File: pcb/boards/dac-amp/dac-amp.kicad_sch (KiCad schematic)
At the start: 10 parts, among them J1 I2S_Input, J2 12V_Input, J3 Front_Left, J4 Front_Right, J5 Rear_Left, J6 Rear_Right, U1 PCM5142, U2 TPA3116D2, U3 TPA3116D2, U4 AMS1117-3.3

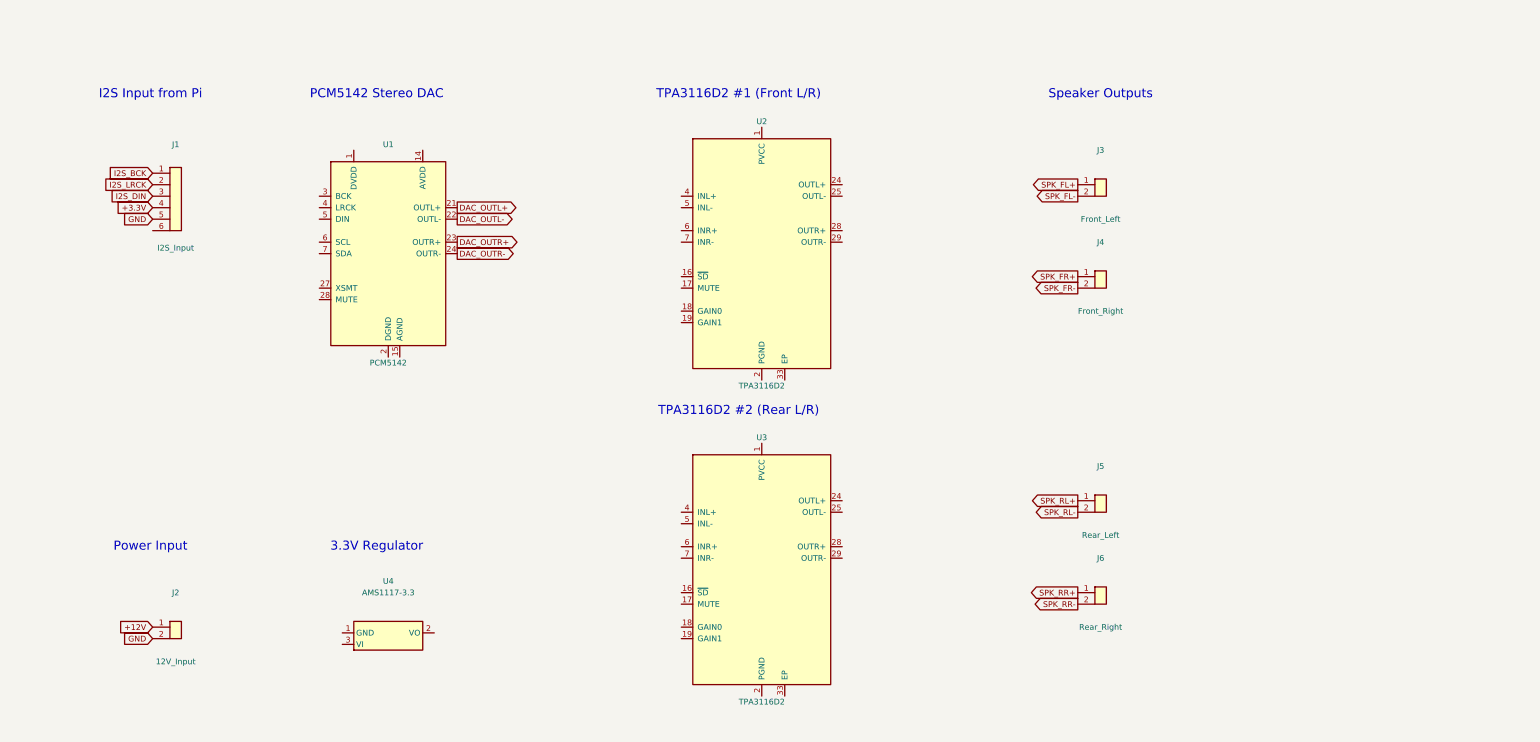
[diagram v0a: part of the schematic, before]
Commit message: Power HAT: Initial PCB layout with component placement
PCB Layout:
- 65mm × 56mm board outline (standard Pi HAT)
- 4× M2.5 mounting holes at corners
- 40-pin GPIO header (J2) positioned for Pi stacking
- Power section (U1 TPS54560, L1, capacitors) on left side
- MCU section (U3 ATtiny85, Y1 crystal) in center
- MOSFET power switching (Q1, Q2, Q3) at bottom
- Optocoupler (U2) for ignition detection

Also includes:
- DAC/Amp HAT schematic complete with I2S, I2C, power wiring
- CAN HAT schematic updates
- Layout scripts for automated component placement
- Updated documentation

Co-Authored-By: Claude Opus 4.5 <noreply@anthropic.com>
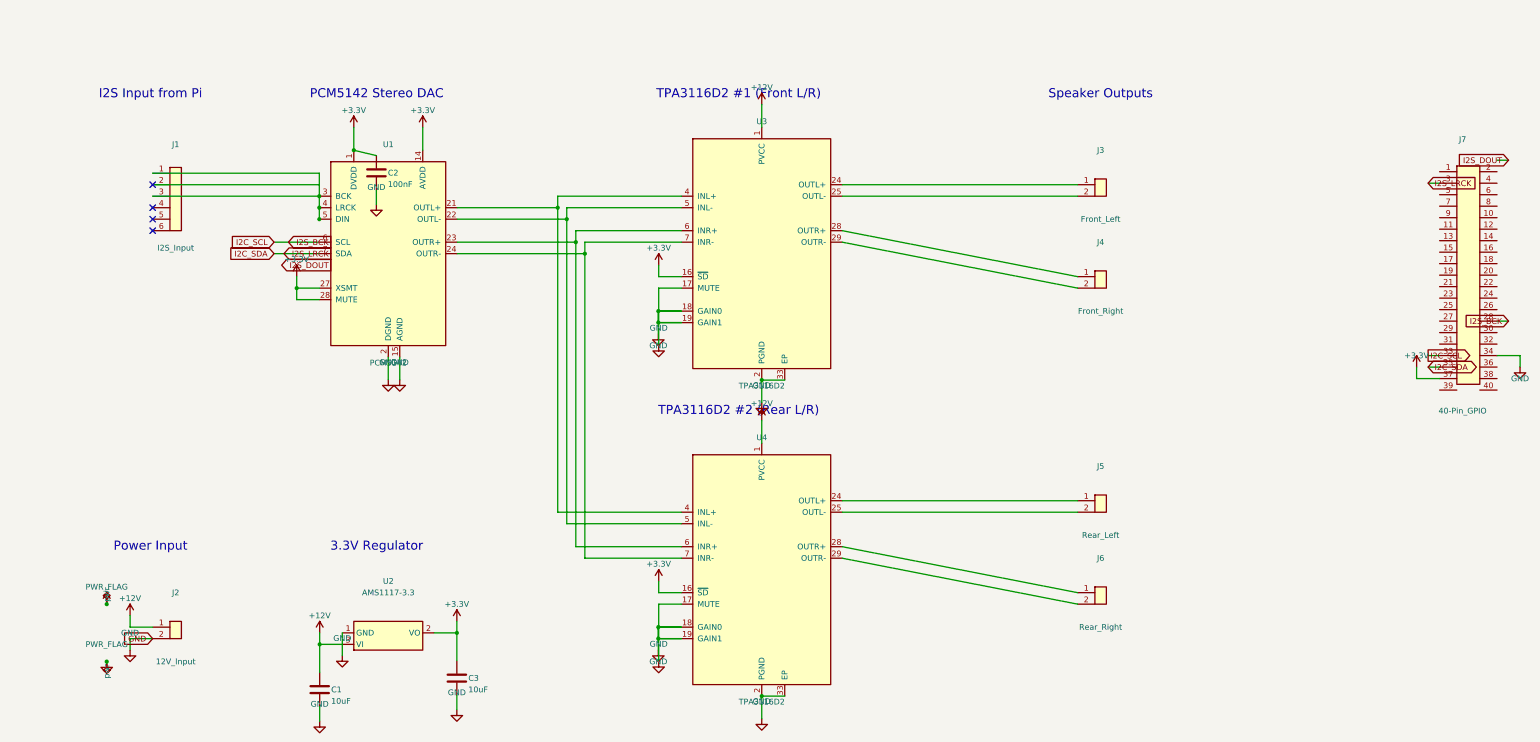
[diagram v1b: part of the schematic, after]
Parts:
- added C1, C3: 10uF, Capacitor_SMD:C_0805_2012Metric, symbol Device:C
- added C2: 100nF, Capacitor_SMD:C_0805_2012Metric, symbol Device:C
- added J7: 40-Pin_GPIO, Connector_PinSocket_2.54mm:PinSocket_2x20_P2.54mm_Vertical, symbol Connector_Generic:Conn_02x20_Odd_Even
- renumbered U4 to U2, U2 to U3, U3 to U4
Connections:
- net DAC_OUTL+ is gone; now on an unnamed net: U1.21 (OUTL+)
- net DAC_OUTL- is gone; now on an unnamed net: U1.22 (OUTL-)
- net DAC_OUTR+ is gone; now on an unnamed net: U1.23 (OUTR+)
- net DAC_OUTR- is gone; now on an unnamed net: U1.24 (OUTR-)
- net I2S_DIN is gone; now on an unnamed net: J1.3 (Pin_3)
- net +12V: now also U2.3 (VI), U3.1 (PVCC), U4.1 (PVCC), C1.1
- net +3.3V: now also U1.1 (DVDD), U1.14 (AVDD), U1.27 (XSMT), U1.28 (MUTE), U2.2 (VO), U3.16 (~{SD}), U4.16 (~{SD}), C2.1, C3.1, J7.37 (Pin_37); no longer J1.4 (Pin_4)
- net GND: now also U1.15 (AGND), U1.2 (DGND), U2.1 (GND), U3.17 (MUTE), U3.18 (GAIN0), U3.19 (GAIN1), U3.2 (PGND), U3.33 (EP), U4.17 (MUTE), U4.18 (GAIN0), U4.19 (GAIN1), U4.2 (PGND), U4.33 (EP), C1.2, C2.2, C3.2, J7.34 (Pin_34); no longer J1.5 (Pin_5)
- net I2S_BCK: now also J7.28 (Pin_28); no longer J1.1 (Pin_1)
- net I2S_LRCK: now also J7.3 (Pin_3); no longer J1.2 (Pin_2)
- net at J5.1 (Pin_1): now also U4.24 (OUTL+)
- net at J5.2 (Pin_2): now also U4.25 (OUTL-)
- net at J4.1 (Pin_1): now also U3.28 (OUTR+)
- net at J4.2 (Pin_2): now also U3.29 (OUTR-)
- net at J6.1 (Pin_1): now also U4.28 (OUTR+)
- net at J6.2 (Pin_2): now also U4.29 (OUTR-)
- net at J3.1 (Pin_1): now also U3.24 (OUTL+)
- net at J3.2 (Pin_2): now also U3.25 (OUTL-)
- net at U3.4 (INL+): now also U4.4 (INL+)
- net at U3.5 (INL-): now also U4.5 (INL-)
- net at U3.6 (INR+): now also U4.6 (INR+)
- net at U3.7 (INR-): now also U4.7 (INR-)
- net at U1.3 (BCK): now also J1.1 (Pin_1), U1.4 (LRCK), U1.5 (DIN)
- net I2C_SCL: now reaches U1.6 (SCL)
- net I2C_SCL: now also J7.33 (Pin_33)
- net I2C_SDA: now reaches U1.7 (SDA)
- net I2C_SDA: now also J7.35 (Pin_35)
- no-connect marks 0 -> 4

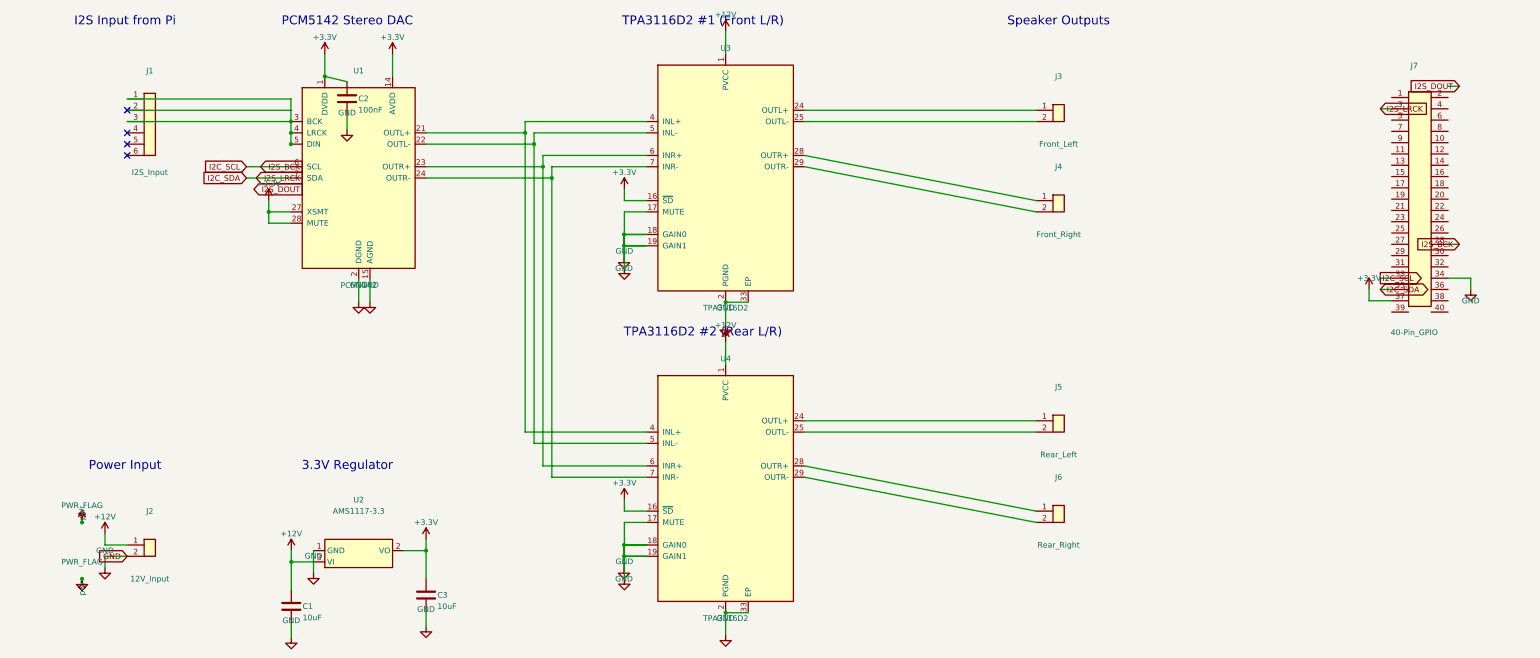
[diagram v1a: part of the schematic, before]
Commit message: CAN HAT + DAC/Amp: PCB layouts started with HAT board outlines
- CAN HAT: PCB created with 65x56mm board outline and M2.5 mounting holes
- DAC/Amp: Fixed remaining ERC errors (XSMT/MUTE tied to 3.3V, J1 no_connect)
- DAC/Amp: Updated TPA3116D2 footprint to ThermalVias variant
- DAC/Amp: PCB created with HAT board outline and mounting holes
- Both boards ready for component placement and routing

Co-Authored-By: Claude Opus 4.5 <noreply@anthropic.com>
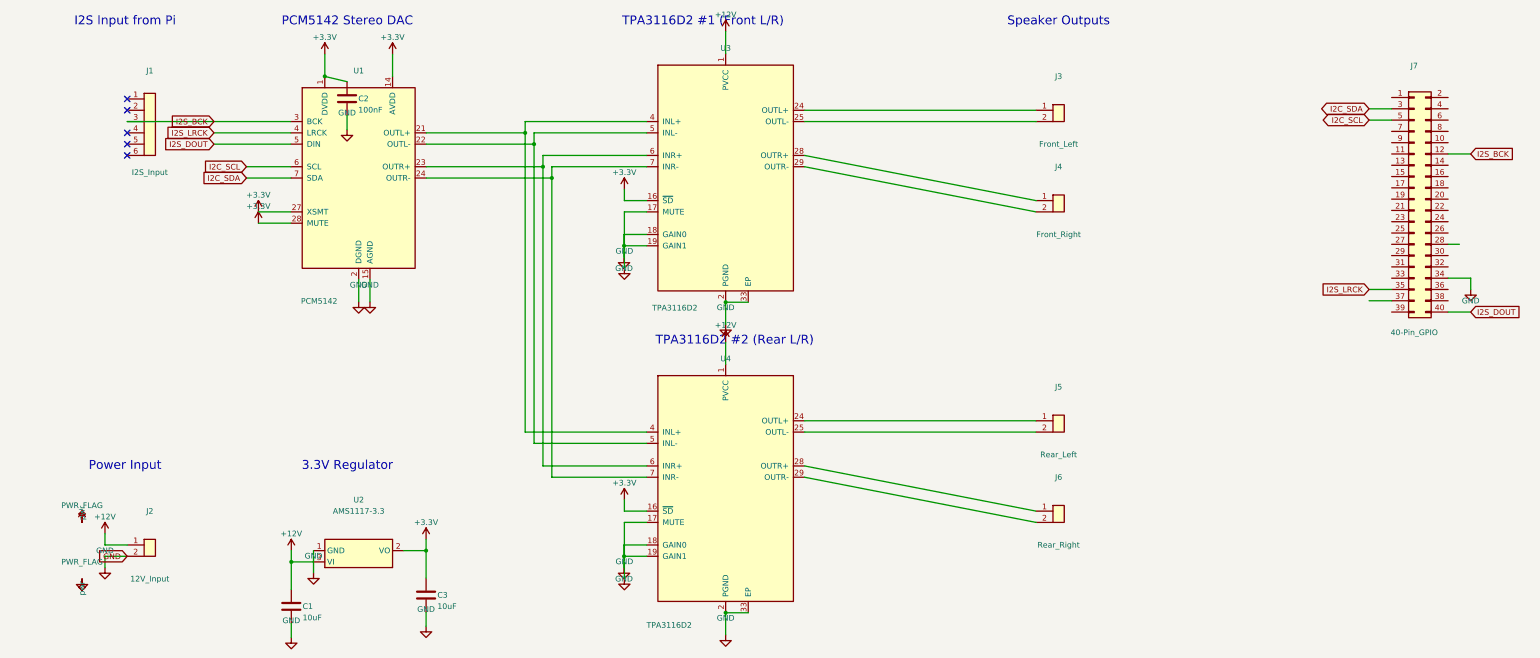
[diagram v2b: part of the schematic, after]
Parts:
- U3, U4: footprint Package_SO:HTSSOP-32-1EP_5.1x11mm_P0.65mm_EP3.4x11mm -> Package_SO:HTSSOP-32-1EP_6.1x11mm_P0.65mm_EP5.2x11mm_Mask4.11x4.36mm_ThermalVias
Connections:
- net +3.3V: no longer J7.37 (Pin_37)
- net I2C_SCL: now also J7.5 (Pin_5); no longer J7.33 (Pin_33)
- net I2C_SDA: now also J7.3 (Pin_3); no longer J7.35 (Pin_35)
- net I2S_BCK: now also J1.3 (Pin_3), J7.12 (Pin_12), U1.3 (BCK); no longer J7.28 (Pin_28)
- net I2S_DOUT: now also J7.40 (Pin_40), U1.5 (DIN)
- net I2S_LRCK: now also J7.35 (Pin_35), U1.4 (LRCK); no longer J7.3 (Pin_3)
- now unconnected: J1.1 (Pin_1)
- no-connect marks 4 -> 5
